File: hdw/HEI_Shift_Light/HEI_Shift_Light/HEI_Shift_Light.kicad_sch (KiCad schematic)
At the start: 0 parts

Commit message: more schematic progress
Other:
- added sheet USB UART Bridge (USB_UART_Bridge.kicad_sch)
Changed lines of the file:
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@@
+	)
+	(sheet
+		(at 36.83 88.9)
+		(size 12.7 3.81)
+		(exclude_from_sim no)
+		(in_bom yes)
+		(on_board yes)
+		(dnp no)
+		(fields_autoplaced yes)
+		(stroke
+			(width 0.1524)
+			(type solid)
+		)
+		(fill
+			(color 0 0 0 0)
+		)
+		(property "Sheetname" "USB UART Bridge"
+			(at 36.83 88.1884 0)
+			(show_name no)
+			(do_not_autoplace no)
+			(effects
+				(font
+					(size 1.27 1.27)
+				)
+				(justify left bottom)
+			)
+		)
+		(property "Sheetfile" "USB_UART_Bridge.kicad_sch"
+			(at 36.83 93.2946 0)
+			(show_name no)
+			(do_not_autoplace no)
+			(effects
+				(font
+					(size 1.27 1.27)
+				)
+				(justify left top)
+			)
+		)
+		(instances
+			(project "HEI_Shift_Light"
+				(path "/288c8230-69eb-4ad9-929d-f4630114196f"
+					(page "6")
+				)
+			)
+		)
 	)
 	(sheet

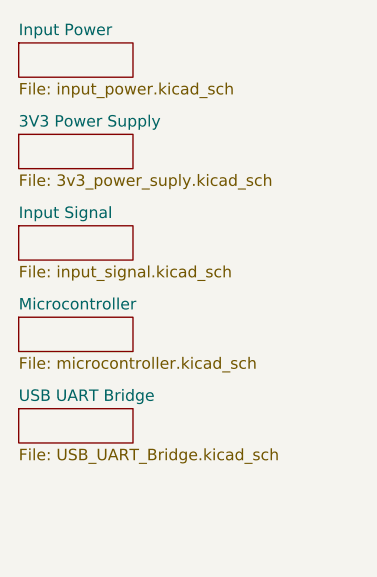
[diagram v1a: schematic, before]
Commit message: populated input protection circuit passive components, updated PIC pinout, added stuff to frequency to voltage converter circuit
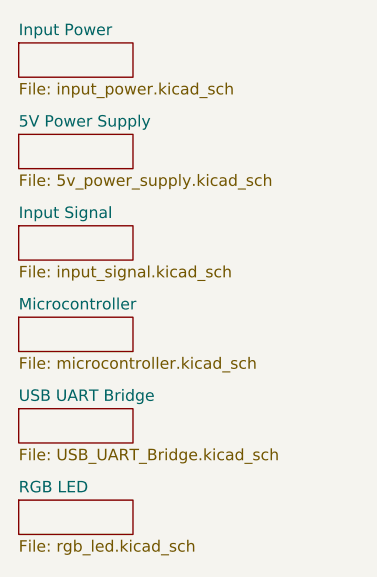
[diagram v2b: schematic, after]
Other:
- sheet 3V3 Power Supply renamed 5V Power Supply
- added sheet RGB LED (rgb_led.kicad_sch)
- sheet 5V Power Supply: file 3v3_power_suply.kicad_sch -> 5v_power_supply.kicad_sch
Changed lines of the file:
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@@
 			(color 0 0 0 0)
 		)
-		(property "Sheetname" "3V3 Power Supply"
+		(property "Sheetname" "5V Power Supply"
 			(at 36.83 57.7084 0)
 			(show_name no)
@@
 			)
 		)
-		(property "Sheetfile" "3v3_power_suply.kicad_sch"
+		(property "Sheetfile" "5v_power_supply.kicad_sch"
 			(at 36.83 62.8146 0)
 			(show_name no)
@@
 				)
 			)
+		)
+	)
+	(sheet
+		(at 36.83 99.06)
+		(size 12.7 3.81)
+		(exclude_from_sim no)
+		(in_bom yes)
+		(on_board yes)
+		(dnp no)
+		(fields_autoplaced yes)
+		(stroke
+			(width 0.1524)
+			(type solid)
+		)
+		(fill
+			(color 0 0 0 0)
+		)
+		(property "Sheetname" "RGB LED"
+			(at 36.83 98.3484 0)
+			(show_name no)
+			(do_not_autoplace no)
+			(effects
+				(font
+					(size 1.27 1.27)
+				)
+				(justify left bottom)
+			)
+		)
+		(property "Sheetfile" "rgb_led.kicad_sch"
+			(at 36.83 103.4546 0)
+			(show_name no)
+			(do_not_autoplace no)
+			(effects
+				(font
+					(size 1.27 1.27)
+				)
+				(justify left top)
+			)
+		)
+		(instances
+			(project "HEI_Shift_Light"
+				(path "/288c8230-69eb-4ad9-929d-f4630114196f"
+					(page "7")
+				)
+			)

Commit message: added more shit, RGD LED, LC input filter
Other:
- company: (none) -> Drew Maatman
- title: (none) -> HEI Shift Light
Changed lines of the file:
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@@
 	(generator_version "10.0")
 	(paper "A")
+	(title_block
+		(title "HEI Shift Light")
+		(date "2026-05-29")
+		(rev "A")
+		(company "Drew Maatman")
+	)
 	(sheet
 		(at 36.83 68.58)
